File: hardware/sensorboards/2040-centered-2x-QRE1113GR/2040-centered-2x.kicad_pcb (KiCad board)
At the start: 2 copper layers, 28 x 54 mm, 8 parts, among them J1 Conn_01x06_Male, U1 QRE1113GR, U2 QRE1113GR

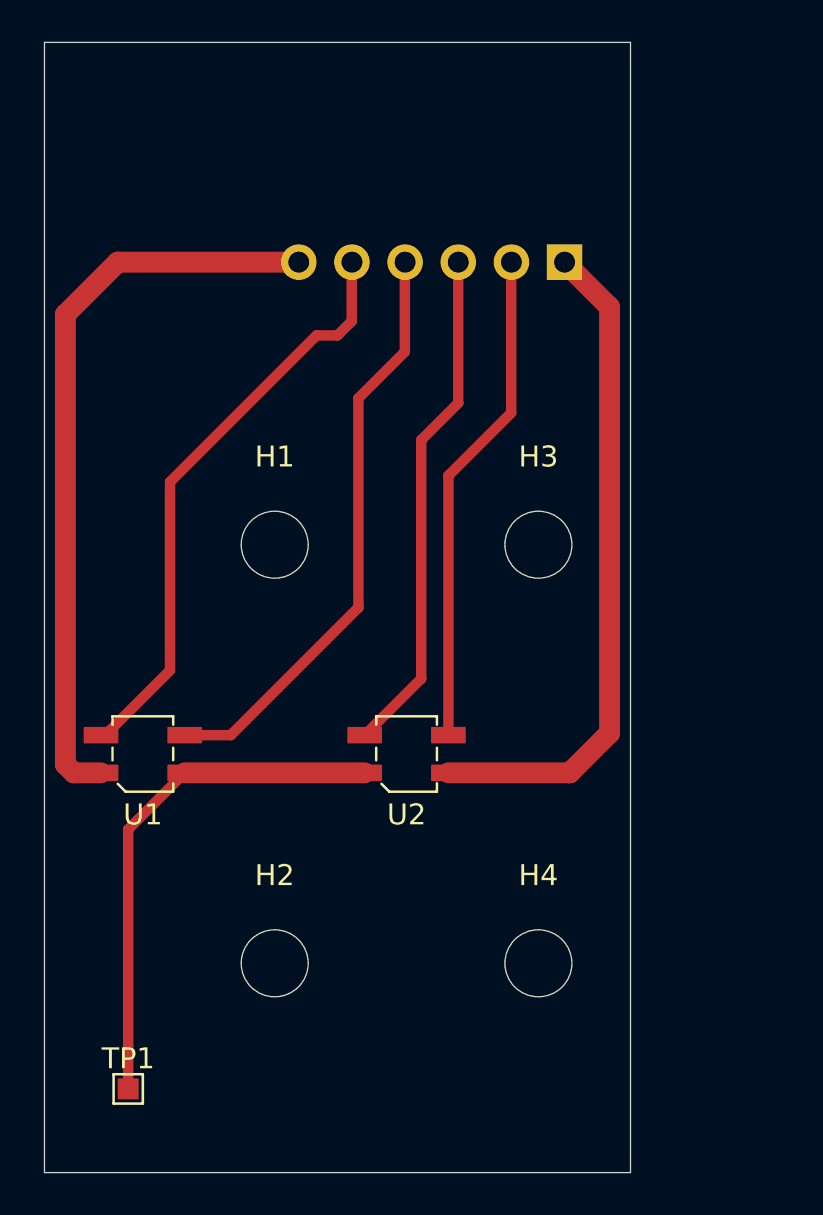
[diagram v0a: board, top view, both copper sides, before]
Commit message: Straight connector Adjusted board size 3D models of parts Raytracing rendering
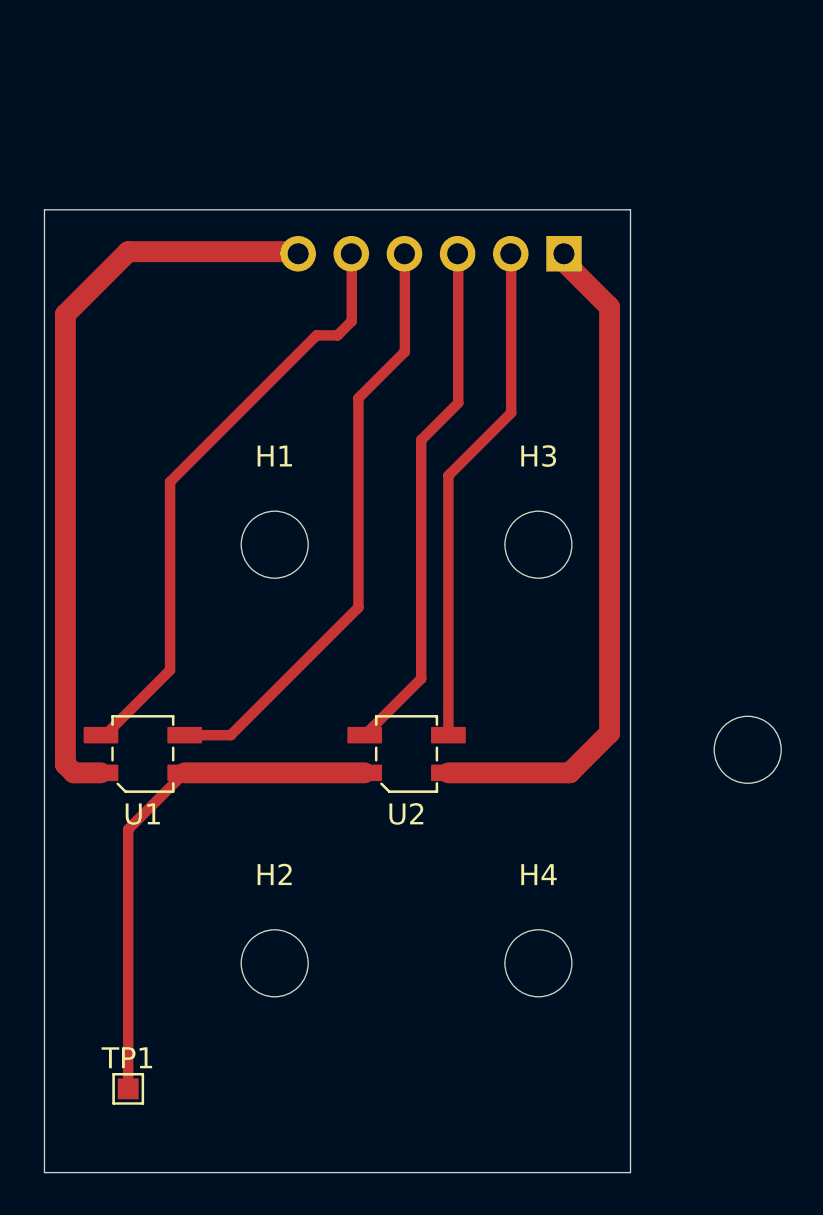
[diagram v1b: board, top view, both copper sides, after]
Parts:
- added ?: , , F.Cu at (151.6, 109.8)
- J1: footprint Pin_Headers:Pin_Header_Angled_1x06_Pitch2.54mm -> Connector_PinHeader_2.54mm:PinHeader_1x06_P2.54mm_Vertical
- moved J1 0.40 mm to (142.8, 86.1)
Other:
- board size 28 x 54 mm -> 28 x 46 mm

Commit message: suggestions from https://pianoclack.com/forum/d/542-update-on-piano-conversion/ for the 2x board too
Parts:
- moved J1 7.50 mm to (135.3, 86.0)
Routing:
- net /NEG: track 31.9 -> 43.2 mm
- net /POS: track 35.3 -> 31.1 mm
- net Net-(U1-Pad3): track 28.4 -> 24.3 mm
- net Net-(U1-Pad4): track 28.4 -> 25.9 mm
- net Net-(U2-Pad3): track 24.0 -> 26.1 mm
- net Net-(TP1-Pad1): track 24.8 -> 26.8 mm
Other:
- board size 28 x 46 mm -> 28.2 x 46 mm
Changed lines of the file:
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@@
   )
   (footprint "Connector_PinHeader_2.54mm:PinHeader_1x06_P2.54mm_Vertical" (layer "B.Cu")
-    (at 142.82 86.1 90)
+    (at 135.32 86 90)
     (descr "Through hole straight pin header, 1x06, 2.54mm pitch, single row")
     (tags "Through hole pin header THT 1x06 2.54mm single row")
@@
     )
   )
-  (gr_rect (start 118 84) (end 146 130) (layer "Edge.Cuts") (width 0.05) (fill none))
-  (segment (start 133.3 110.9) (end 124.7 110.9) (width 1) (layer "F.Cu") (net 1))
-  (segment (start 124.7 110.9) (end 122 113.6) (width 0.5) (layer "F.Cu") (net 1))
-  (segment (start 122 113.6) (end 122 126) (width 0.5) (layer "F.Cu") (net 1))
-  (segment (start 137.3 110.9) (end 143.1 110.9) (width 1) (layer "F.Cu") (net 2))
-  (segment (start 145 88.65) (end 142.85 86.5) (width 1) (layer "F.Cu") (net 2))
-  (segment (start 143.1 110.9) (end 145 109) (width 1) (layer "F.Cu") (net 2))
-  (segment (start 145 109) (end 145 88.65) (width 1) (layer "F.Cu") (net 2))
-  (segment (start 119 110.5) (end 119 89) (width 1) (layer "F.Cu") (net 3))
-  (segment (start 119 89) (end 122 86) (width 1) (layer "F.Cu") (net 3))
-  (segment (start 120.7 110.9) (end 119.4 110.9) (width 1) (layer "F.Cu") (net 3))
-  (segment (start 122 86) (end 129.65 86) (width 1) (layer "F.Cu") (net 3))
-  (segment (start 119.4 110.9) (end 119 110.5) (width 1) (layer "F.Cu") (net 3))
-  (segment (start 137.3 96.7) (end 140.3 93.7) (width 0.5) (layer "F.Cu") (net 4))
-  (segment (start 137.3 109.1) (end 137.3 96.7) (width 0.5) (layer "F.Cu") (net 4))
-  (segment (start 140.3 93.7) (end 140.3 86.375) (width 0.5) (layer "F.Cu") (net 4))
-  (segment (start 133.3 109.1) (end 136 106.4) (width 0.5) (layer "F.Cu") (net 5))
-  (segment (start 136 95) (end 137.77 93.23) (width 0.5) (layer "F.Cu") (net 5))
-  (segment (start 136 106.4) (end 136 95) (width 0.5) (layer "F.Cu") (net 5))
-  (segment (start 137.77 93.23) (end 137.77 86.375) (width 0.5) (layer "F.Cu") (net 5))
-  (segment (start 126.9 109.1) (end 133 103) (width 0.5) (layer "F.Cu") (net 6))
-  (segment (start 135.22 90.78) (end 135.22 86.375) (width 0.5) (layer "F.Cu") (net 6))
-  (segment (start 133 93) (end 135.22 90.78) (width 0.5) (layer "F.Cu") (net 6))
-  (segment (start 124.7 109.1) (end 126.9 109.1) (width 0.5) (layer "F.Cu") (net 6))
-  (segment (start 133 103) (end 133 93) (width 0.5) (layer "F.Cu") (net 6))
-  (segment (start 120.7 109.1) (end 120.9 109.1) (width 0.5) (layer "F.Cu") (net 7))
-  (segment (start 131 90) (end 132 90) (width 0.5) (layer "F.Cu") (net 7))
-  (segment (start 132.68 89.32) (end 132.68 86.375) (width 0.5) (layer "F.Cu") (net 7))
-  (segment (start 132 90) (end 132.68 89.32) (width 0.5) (layer "F.Cu") (net 7))
-  (segment (start 124 106) (end 124 97) (width 0.5) (layer "F.Cu") (net 7))
-  (segment (start 124 97) (end 131 90) (width 0.5) (layer "F.Cu") (net 7))
-  (segment (start 120.9 109.1) (end 124 106) (width 0.5) (layer "F.Cu") (net 7))
+  (gr_rect (start 117.9 84) (end 146.1 130) (layer "Edge.Cuts") (width 0.05) (fill none))
+  (segment (start 122 118.3) (end 129.4 110.9) (width 0.5) (layer "F.Cu") (net 1))
+  (segment (start 122 126) (end 122 118.3) (width 0.5) (layer "F.Cu") (net 1))
+  (segment (start 129.4 110.9) (end 133.3 110.9) (width 0.5) (layer "F.Cu") (net 1))
+  (segment (start 124.7 110.9) (end 129.4 110.9) (width 0.5) (layer "F.Cu") (net 1))
+  (segment (start 135.32 86) (end 145.47548 86) (width 1) (layer "F.Cu") (net 2))
+  (segment (start 137.3 110.9) (end 139.5 110.9) (width 0.5) (layer "F.Cu") (net 2))
+  (segment (start 145.47548 110.9) (end 139.5 110.9) (width 1) (layer "F.Cu") (net 2))
+  (segment (start 145.47548 86) (end 145.47548 110.9) (width 1) (layer "F.Cu") (net 2))
+  (segment (start 122.62 86) (end 118.7 86) (width 1) (layer "F.Cu") (net 3))
+  (segment (start 118.52452 86.17548) (end 118.52452 110.9) (width 1) (layer "F.Cu") (net 3))
+  (segment (start 120.7 110.9) (end 118.52452 110.9) (width 0.5) (layer "F.Cu") (net 3))
+  (segment (start 118.7 86) (end 118.52452 86.17548) (width 1) (layer "F.Cu") (net 3))
+  (segment (start 135.4 109.1) (end 137.3 109.1) (width 0.5) (layer "F.Cu") (net 4))
+  (segment (start 133.999519 87.219519) (end 133.999519 107.699519) (width 0.5) (layer "F.Cu") (net 4))
+  (segment (start 133.999519 107.699519) (end 135.4 109.1) (width 0.5) (layer "F.Cu") (net 4))
+  (segment (start 132.78 86) (end 133.999519 87.219519) (width 0.5) (layer "F.Cu") (net 4))
+  (segment (start 133.3 89.06) (end 133.3 109.1) (width 0.5) (layer "F.Cu") (net 5))
+  (segment (start 130.24 86) (end 133.3 89.06) (width 0.5) (layer "F.Cu") (net 5))
+  (segment (start 124.7 109.1) (end 124.7 89.2) (width 0.5) (layer "F.Cu") (net 6))
+  (segment (start 127.7 86.2) (end 127.7 86) (width 0.5) (layer "F.Cu") (net 6))
+  (segment (start 124.7 89.2) (end 127.7 86.2) (width 0.5) (layer "F.Cu") (net 6))
+  (segment (start 122.6 109.1) (end 120.7 109.1) (width 0.5) (layer "F.Cu") (net 7))
+  (segment (start 125.16 86.2) (end 124.00048 87.35952) (width 0.5) (layer "F.Cu") (net 7))
+  (segment (start 124.00048 107.69952) (end 122.6 109.1) (width 0.5) (layer "F.Cu") (net 7))
+  (segment (start 124.00048 87.35952) (end 124.00048 107.69952) (width 0.5) (layer "F.Cu") (net 7))
 )
